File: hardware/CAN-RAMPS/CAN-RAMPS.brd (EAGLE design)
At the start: 59.7 x 15.2 mm, 31 parts, among them Q1 12MHZ, U1 MCP2515(MCP2510)ML, U2 MCP2551, U4 ATTINY816M

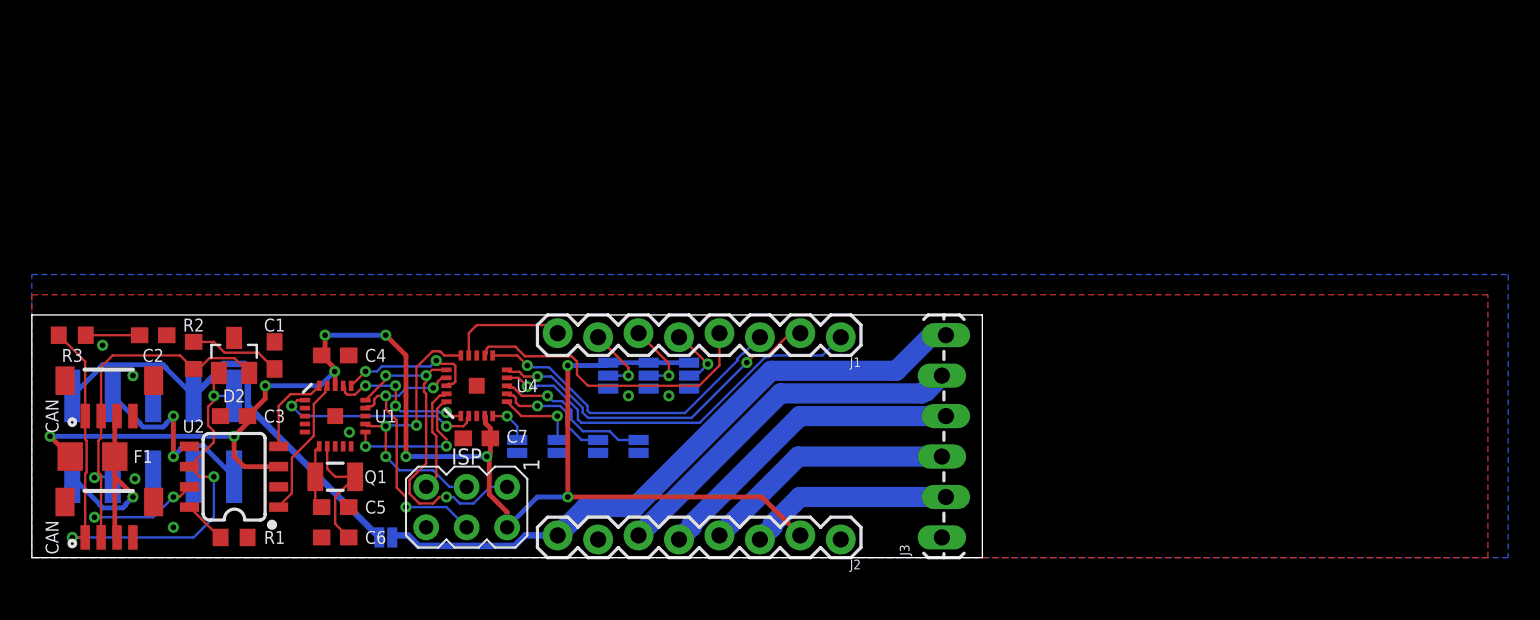
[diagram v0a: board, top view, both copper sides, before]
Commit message: Added mounting tabs
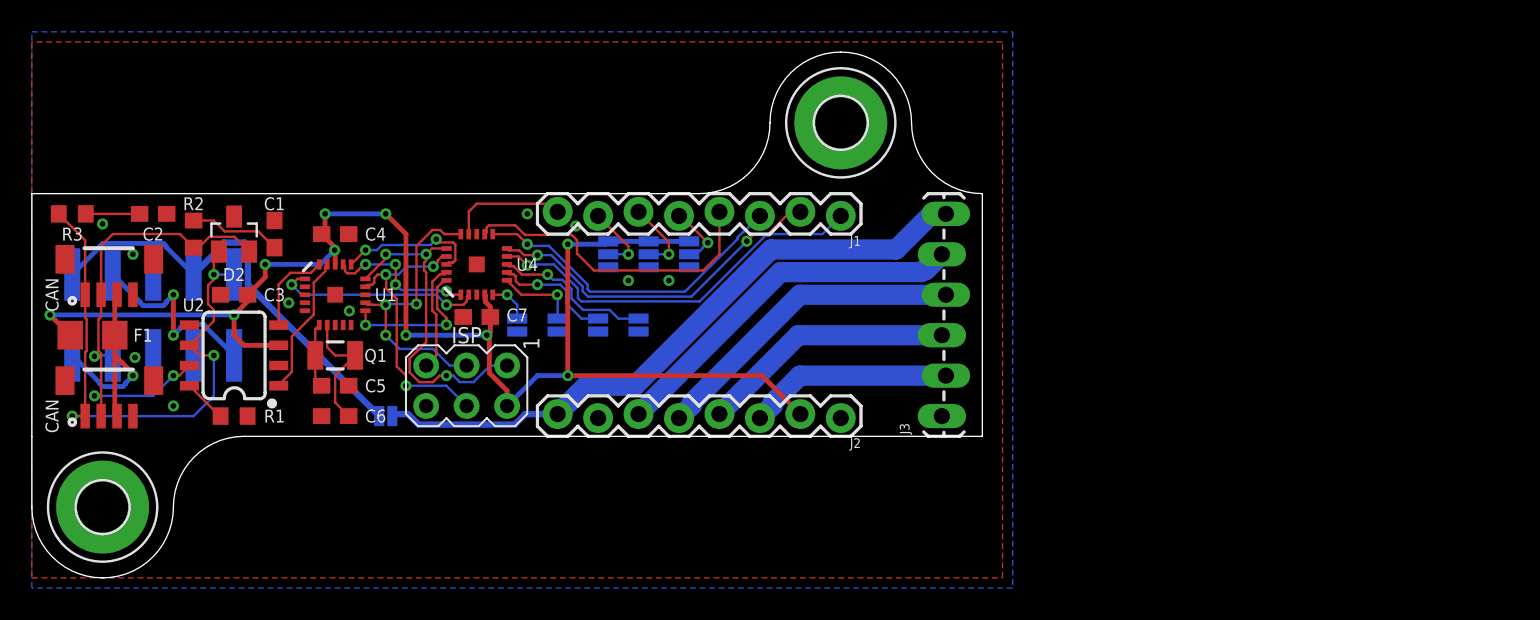
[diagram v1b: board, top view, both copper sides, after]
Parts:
- added H1, H2: MOUNT-PAD-ROUND3.2, holes:3,2-PAD
- moved C1 7.62 mm to (15.2, 20.3)
- moved C3 7.62 mm to (12.7, 16.5)
- moved C4 7.62 mm to (19.1, 20.3)
- moved C6 7.62 mm to (19.1, 8.89)
- moved CAN-IN 7.62 mm to (3.81, 17.8)
- moved D2 7.62 mm to (12.7, 20.3)
- moved F1 7.62 mm to (3.81, 14.0)
- moved J2 7.62 mm to (50.8, 8.89)
- moved J3 7.62 mm to (57.1, 8.89)
- moved MOT_PWR 7.62 mm to (22.2, 8.89)
- moved MS1 7.62 mm to (36.2, 19.1)
- moved MS2 7.62 mm to (38.7, 19.1)
- moved MS3 7.62 mm to (41.3, 19.1)
- moved R1 7.62 mm to (12.7, 8.89)
- moved R2 7.62 mm to (10.2, 20.3)
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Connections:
- net GND: now also H1.B3,2, H2.B3,2
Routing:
- net !RST!: track 19.2 -> 19.9 mm
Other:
- board size 59.7 x 15.2 mm -> 59.7 x 33 mm
